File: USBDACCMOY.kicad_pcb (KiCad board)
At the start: 2 copper layers, 49.6 x 77.8 mm, 54 parts, among them CON1 GND_CONNECTORSMD, IC1 OPA2134P, J1 USB, Q1 12MHz, U1 NMA0512SC, U2 PCM2707C

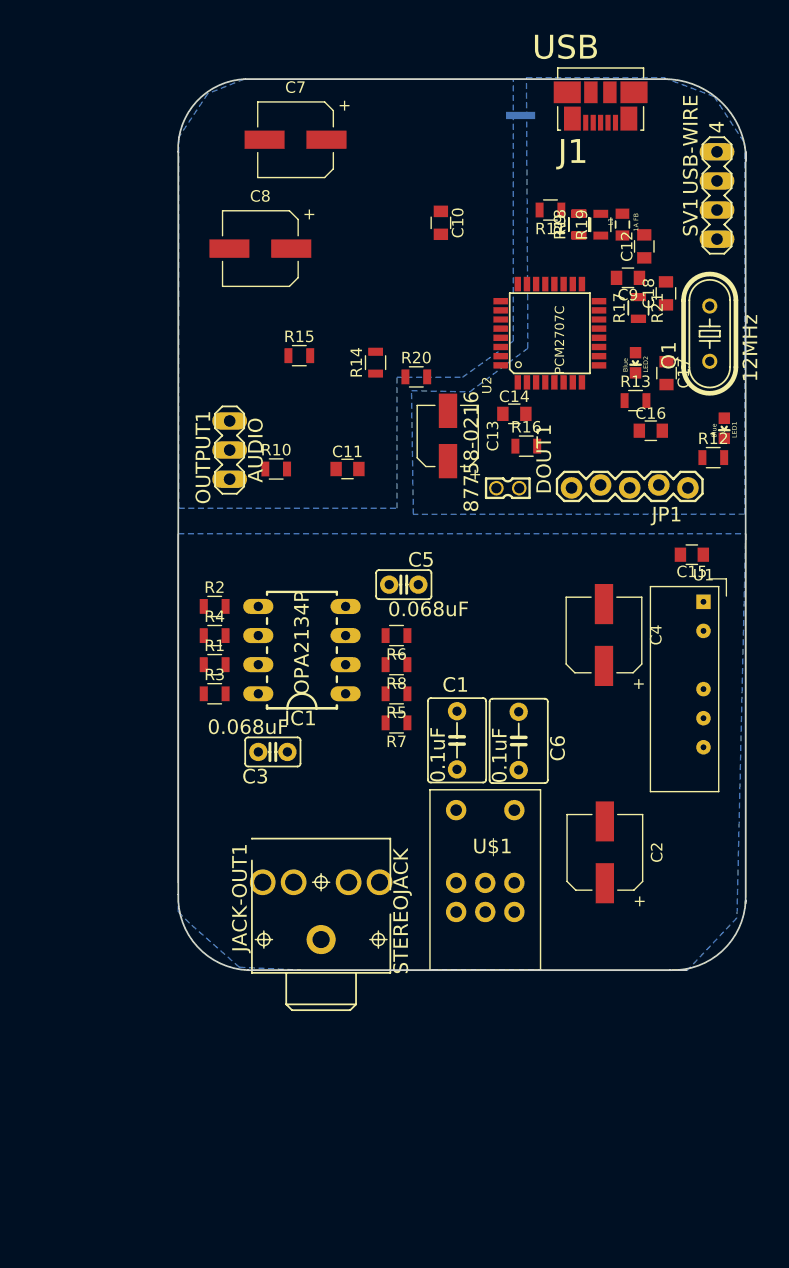
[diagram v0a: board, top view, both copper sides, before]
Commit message: Updated to kicad 5.0 and started routing.
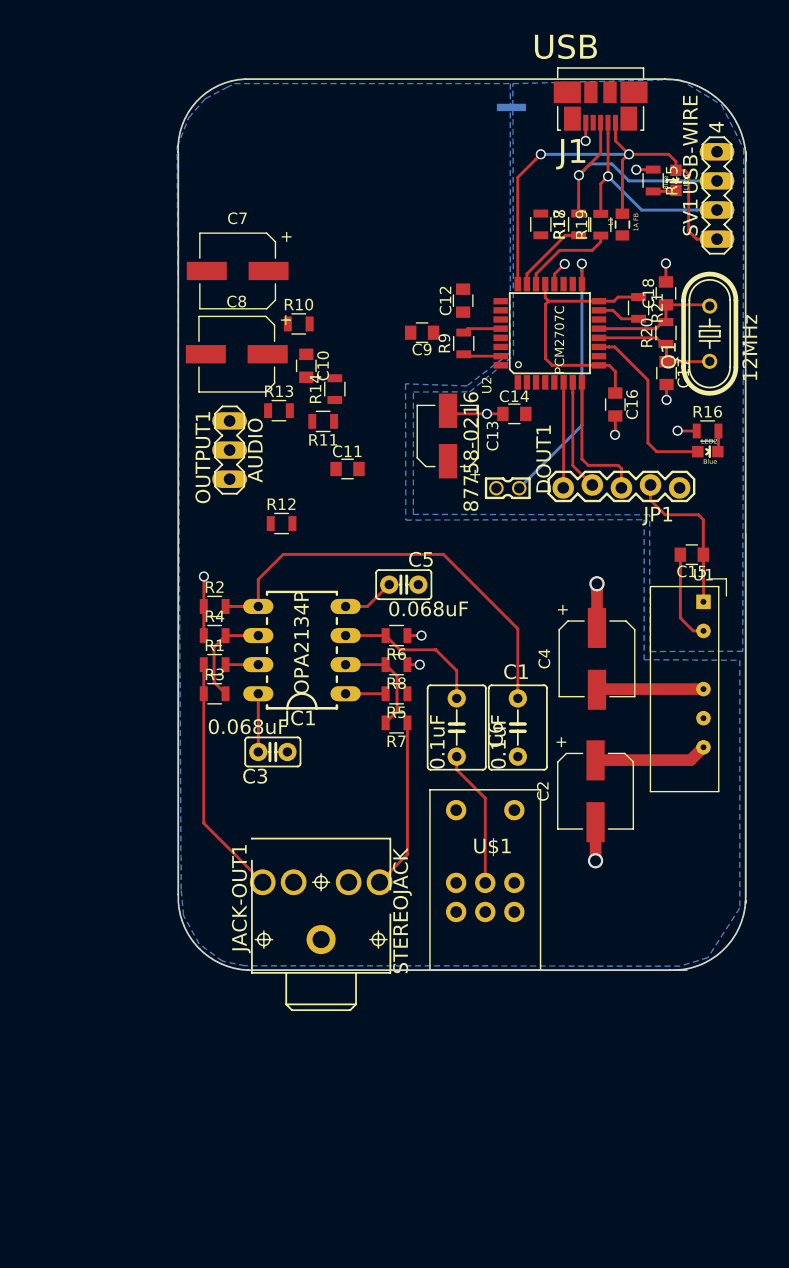
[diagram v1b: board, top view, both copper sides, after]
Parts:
- moved R12 38.1 mm to (124.0, 92.7)
- moved R15 34.5 mm to (156.4, 62.8), turned to 270 degrees
- moved R13 31.1 mm to (123.8, 82.9)
- moved R11 27.1 mm to (127.6, 83.8)
- moved R20 22.1 mm to (157.6, 76.1), turned to 90 degrees
- moved LED1 22.0 mm to (158.4, 62.8)
- moved C9 18.6 mm to (136.3, 76.1)
- moved C10 17.1 mm to (126.2, 79.0)
- moved C12 16.5 mm to (139.9, 73.3)
- moved R16 15.9 mm to (161.2, 84.7)
- moved R9 14.4 mm to (139.9, 77.0)
- moved R10 12.8 mm to (125.5, 75.3)
- moved C7 12.5 mm to (120.2, 70.7)
- moved R17 11.2 mm to (146.6, 66.6), turned to 270 degrees
- moved LED2 10.0 mm to (161.2, 86.5), turned to 270 degrees
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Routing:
- net VBUS: track 0.00 -> 56.5 mm, vias 0 -> 2
- net /CMOY/L+: track 0.00 -> 37.5 mm
- net GND: track 0.00 -> 24.4 mm, vias 0 -> 8
- net /PCM2707/N$6: track 0.00 -> 23.6 mm, vias 0 -> 1
- net VDD: track 0.00 -> 23.2 mm
- net /PCM2707/D+: track 0.00 -> 21.8 mm, vias 0 -> 1
- net OUTPUT_L: track 0.00 -> 21.1 mm
- net /PCM2707/D-: track 0.00 -> 19.0 mm, vias 0 -> 1
- net AGND: track 0.00 -> 17.9 mm, vias 0 -> 5
- net /PCM2707//SSPND: track 0.00 -> 15.6 mm
- net V+: track 0.00 -> 15.0 mm
- net OUTPUT_R: track 0.00 -> 14.9 mm
- net V-: track 0.00 -> 13.9 mm
- net /CMOY/R+: track 0.00 -> 13.4 mm
- net /PCM2707/N$5: track 0.00 -> 12.2 mm
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
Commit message: Updated Design Files
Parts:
- removed U$1: ~, CMOY:AUDIO-POTS_ALPS_RK0971221Z0X
- added C19: C, Capacitors_SMD:C_0805_HandSoldering, F.Cu at (145.9, 121.4)
- added L2: L, Capacitors_SMD:C_0805_HandSoldering, F.Cu at (148.3, 126.3)
- added M1: AUDIO-POTS_ALPS_RK0971221Z05, PCM2707:AUDIO-POTS_ALPS_RK0971221Z0X, F.Cu at (136.5, 144.6)
- added SYM1: SYM_ESD_Small, Symbols:ESD-Logo_6.6x6mm_SilkScreen, F.Cu at (112.3, 81.5)
- IC1: footprint CMOY:DIL-8 -> SMD_Packages:SOIC-8-N
- moved C1 37.9 mm to (128.0, 144.6)
- moved C15 30.8 mm to (131.3, 83.8), turned to 90 degrees
- moved C6 28.1 mm to (127.9, 136.2)
- moved L1 26.9 mm to (133.1, 83.8)
- moved C7 25.8 mm to (113.9, 95.7), turned to 270 degrees
- moved R9 25.8 mm to (121.5, 95.0), turned to 0 degrees
- moved C12 24.7 mm to (126.6, 94.2)
- moved JACK-OUT1 24.7 mm to (113.4, 152.1)
- moved C13 24.7 mm to (125.0, 105.8), turned to 270 degrees
- moved CON1 24.6 mm to (131.2, 77.0)
- moved C5 24.6 mm to (121.2, 118.6)
- moved J1 24.6 mm to (138.4, 78.3)
- moved LED1 24.6 mm to (145.0, 83.4)
- moved R16 24.6 mm to (147.7, 105.2)
- moved R18 24.6 mm to (136.5, 87.2)
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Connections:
- C15 pad 1: VBUS -> Net-(C15-Pad1)
- L1 pad 1: VBUS -> Net-(C15-Pad1)
- U1 pad 1: VBUS -> Net-(C19-Pad1)
- U2 pad 24: VBUS -> Net-(C15-Pad1)
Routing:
- net INPUT_R: track 0.00 -> 83.1 mm
- net INPUT_L: track 0.00 -> 81.2 mm
- net VBUS: track 56.5 -> 105.3 mm
- net V+: track 15.0 -> 59.6 mm, vias 0 -> 1
- net /PCM2707/N$21: track 0.00 -> 27.8 mm
- net V-: track 13.9 -> 38.4 mm
- net /PCM2707/N$23: track 3.37 -> 26.0 mm
- net AGND: track 17.9 -> 35.3 mm, vias 5 -> 13
- net Net-(L2-Pad1): track 0.00 -> 16.8 mm
- net /CMOY/VOLUME-OUT-L: track 0.00 -> 13.4 mm
- net /CMOY/R+: track 13.4 -> 24.2 mm
- net Net-(C15-Pad1): track 0.00 -> 9.47 mm
- net VDD: track 23.2 -> 31.6 mm
- net Net-(C19-Pad1): track 0.00 -> 7.25 mm
- net /PCM2707/N$4: track 0.00 -> 6.78 mm
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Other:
- board size 49.6 x 77.8 mm -> 49.5 x 77.8 mm
- net class Default: clearance 0.254 -> 0.19
- net class VCC added: clearance 0.19, trace_width 0.512, via_dia 0.889, via_drill 0.635
- rule trace_clearance: 0.254 -> 0.19
- board text added: "DRILL STACK ============================= T1 0.51mm 0.020” (5 holes) T2 0.64mm 0.025” (32 holes) T3 0.81mm 0.032” (10 holes) T4 0.90mm 0.035” (2 holes) T5 1.02mm 0.040” (20 holes) T6 1.50mm 0.059” (5 holes) Total plated holes count 74 ============================="
- board text added: "NOTES: UNLESS OTHERWISE SPECIFIED. 1. SURFACE FINISH: • HASL LEAD-FREE 2. PCB DETAILS: • 2 LAYER • 1.6MM ±0.2. • BLACK • FR4 LAMINATE AND PREPREG TO BE IN ACCORDANCE WITH IPC-4101/23 OR IPC-4101/24 3. COPPER WEIGHT: • 1 OZ APPLIED IN ACCORDANCE WITH IPC-4562. COPPER WEIGHTS ARE TO BE CONSIDERED FINISHED. 4. SILKSCREEN IDENT: • WHITE • TOP SIDE ONLY"
